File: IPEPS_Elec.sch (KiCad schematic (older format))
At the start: 34 parts

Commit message: replace the OR gate by transistors
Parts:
- removed U?: CD74HCT4075E, symbol 74xGxx:74LVC1G332
- added Q? (x2): BC547, Package_TO_SOT_THT:TO-92_Inline, symbol Transistor_BJT:BC547
- added R? (x4): 47k, symbol Device:R_Small
- added R?: 100k, symbol Device:R_Small
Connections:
- wire segments 74 -> 78
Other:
- moved on the sheet: BT?, C?, D?, Q?, R?, SW?, U?A, U?B

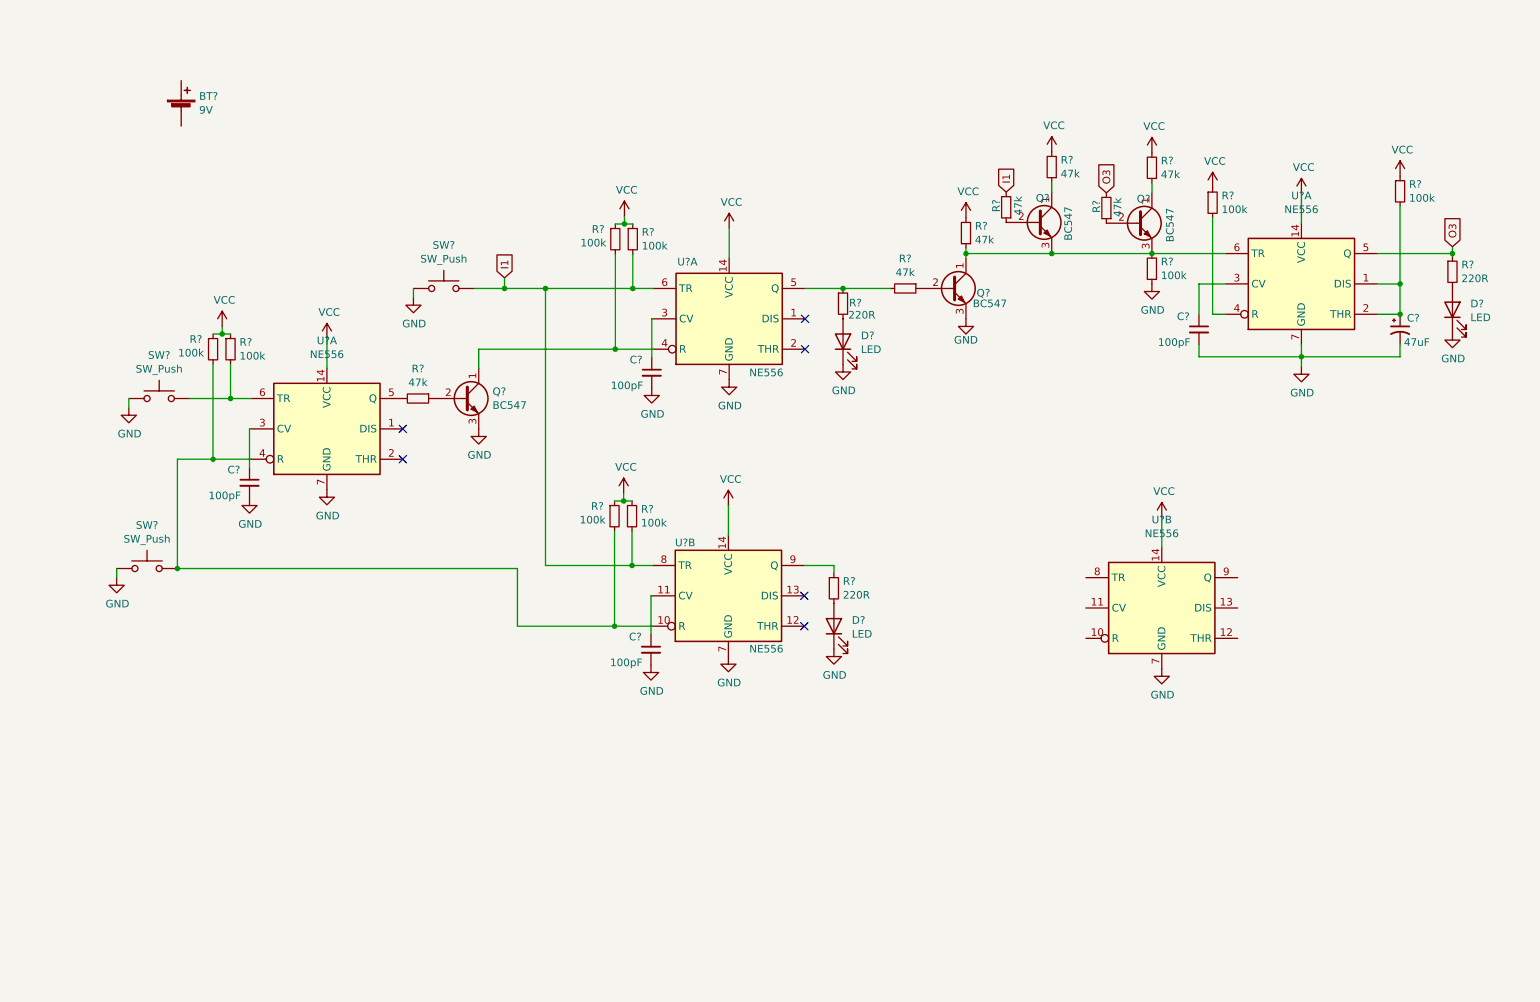
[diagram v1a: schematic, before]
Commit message: remove TTL gates and wire up the astable 555
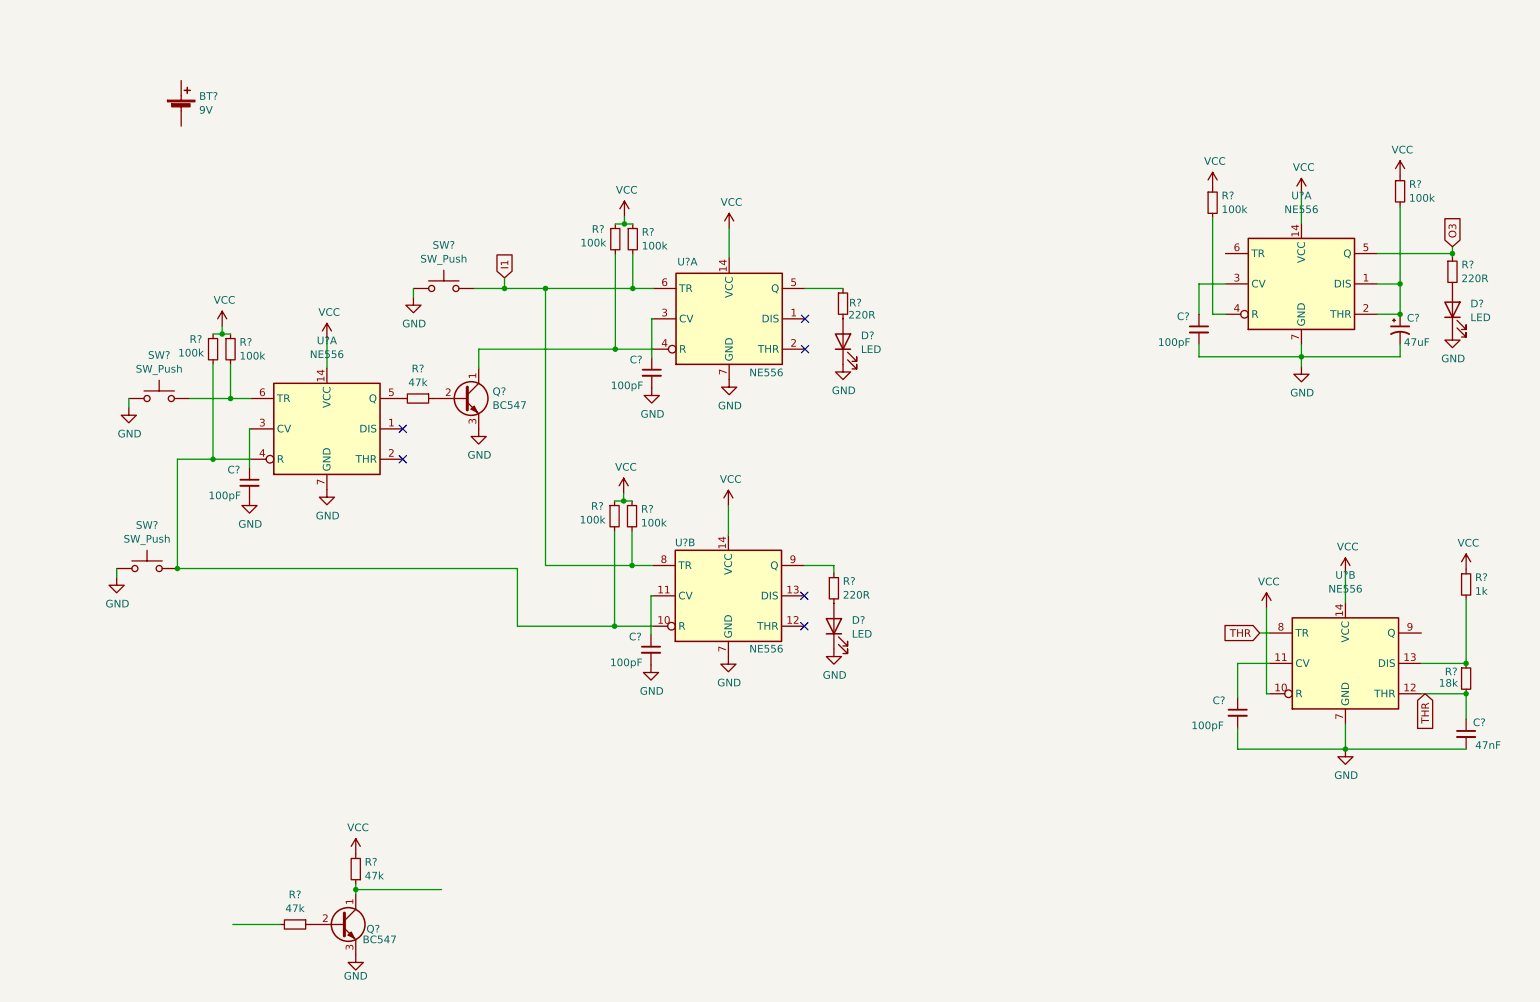
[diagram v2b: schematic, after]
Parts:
- removed Q? (x2): BC547, Package_TO_SOT_THT:TO-92_Inline, symbol Transistor_BJT:BC547
- removed R? (x4): 47k, symbol Device:R_Small
- removed R?: 100k, symbol Device:R_Small
- added C?: 47nF, symbol Device:C_Small
- added C?: 100pF, symbol Device:C_Small
- added R?: 1k, symbol Device:R_Small
- added R?: 18k, symbol Device:R_Small
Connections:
- net GND: now also C?.2, C?.2
- net VCC: now also U?.10 (R), R?.1
- net at R?.1, U?.5 (Q): no longer R?.2
- net at U?.11 (CV): now also C?.1
- net THR: now reaches U?.12 (THR)
- net THR: now also U?.8 (TR), C?.1, R?.2
- net at U?.13 (DIS): now also R?.1, R?.2
- net at Q?.1 (C), R?.1: no longer U?.6 (TR)
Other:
- moved on the sheet: Q?, R?, U?B

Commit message: wire up the tc4428 + add buzzer + wire OR gate
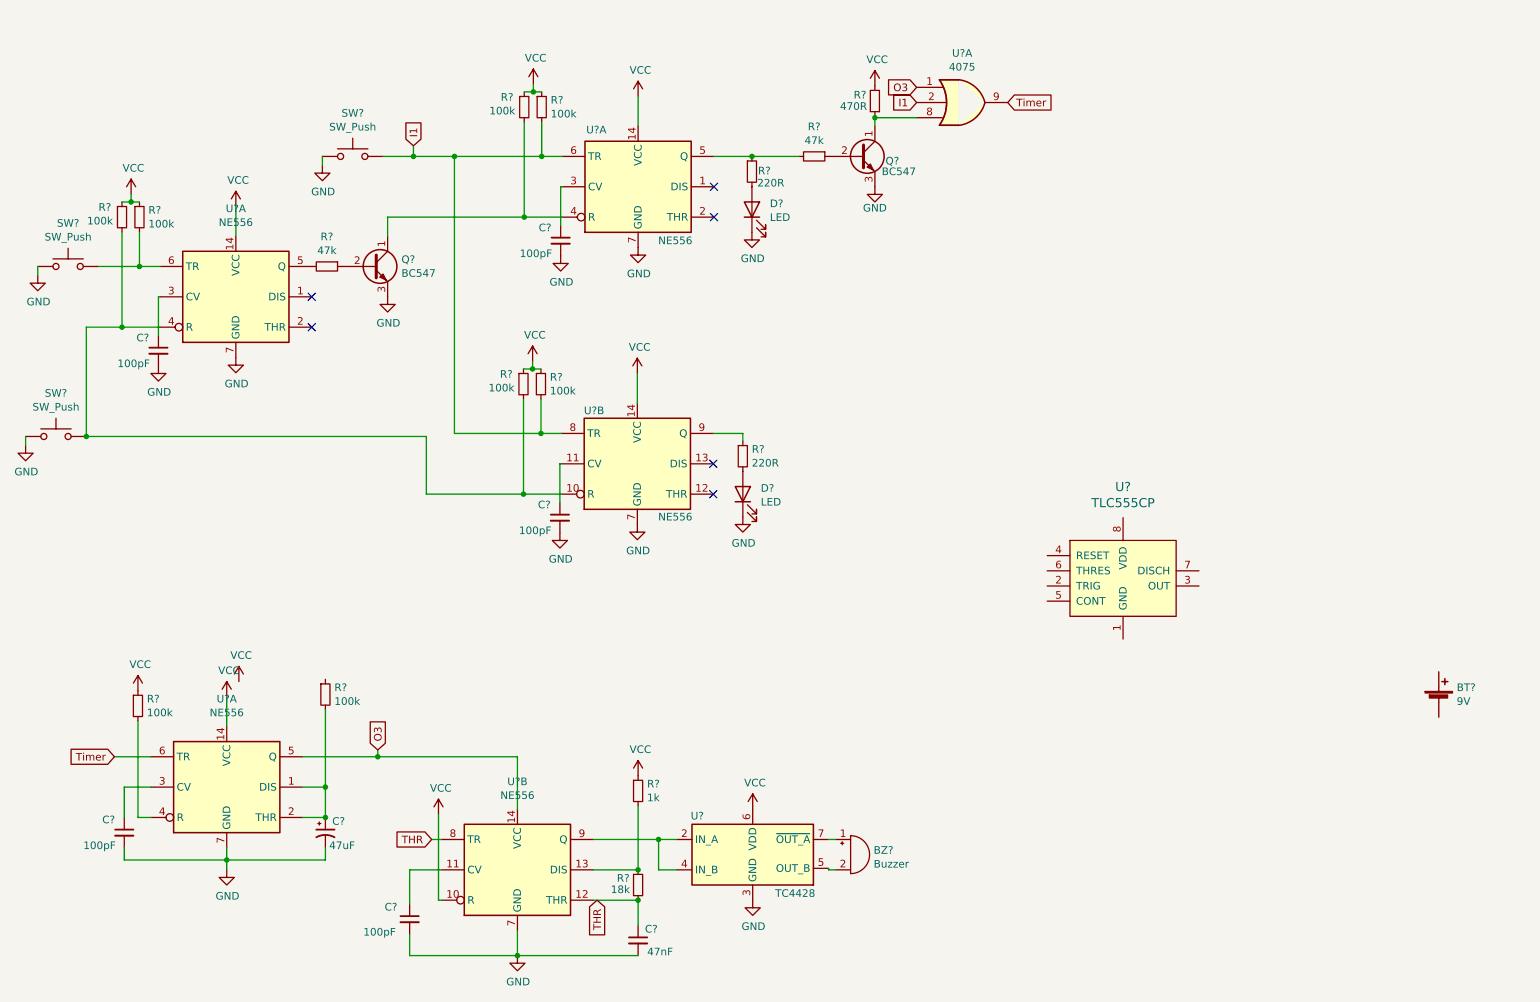
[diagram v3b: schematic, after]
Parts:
- removed D?: LED, symbol Device:LED
- removed R?: 220R, symbol Device:R_Small
- added BZ?: Buzzer, symbol Device:Buzzer
- added U?: TC4428, Package_DIP:DIP-8_W7.62mm, symbol labo2:TC4428
- added U?: 4075, symbol 4xxx:4075
- added U?: TLC555CP, digikey-footprints:DIP-8_W7.62mm, symbol dk_Clock-Timing-Programmable-Timers-and-Oscillators:TLC555CP
- R?: value 47k -> 470R
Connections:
- net GND: now also U?.3 (GND)
- net I1: now also U?.2
- net O3: now also U?.14 (VCC), U?.1
- net VCC: now also U?.6 (VDD); no longer R?.1, U?.14 (VCC)
- net at R?.1, U?.5 (Q): now also R?.2
- net at U?.9 (Q): now also U?.2 (IN_A), U?.4 (IN_B)
- net Timer: now reaches U?.6 (TR)
- net Timer: now also U?.9
- net at Q?.1 (C), R?.1: now also U?.8
- new net: U?.1 (NC), U?.8 (NC)
- new net: BZ?.2 (+), U?.5 (OUT_B)
- new net: BZ?.1 (-), U?.7 (~OUT_A)
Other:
- moved on the sheet: BT?, C?, D?, Q?, R?, SW?, U?A, U?B

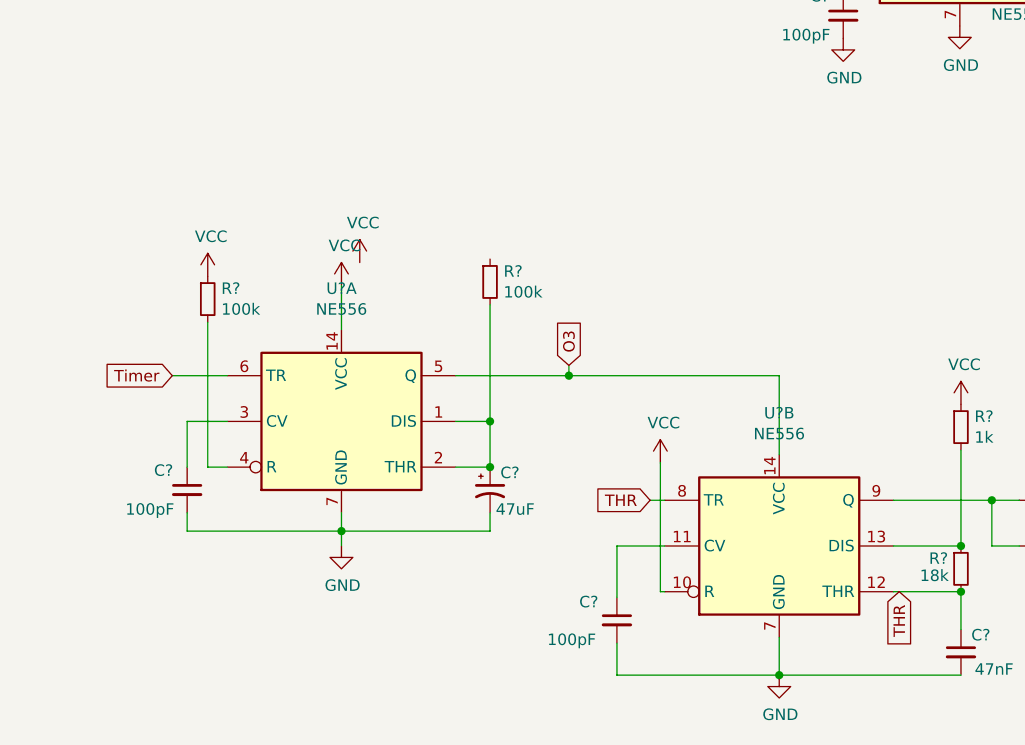
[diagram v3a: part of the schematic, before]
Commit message: add an NPN to power up astable
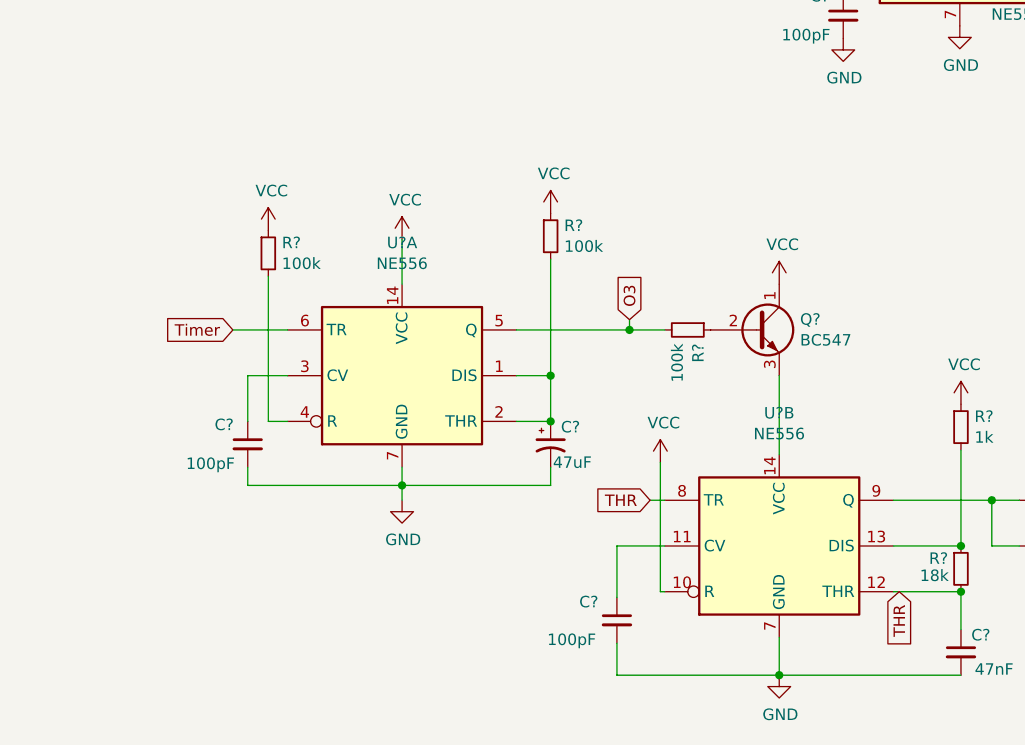
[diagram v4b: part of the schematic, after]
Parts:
- added Q?: BC547, Package_TO_SOT_THT:TO-92_Inline, symbol Transistor_BJT:BC547
- added R?: 100k, symbol Device:R_Small
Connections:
- net O3: now also R?.2; no longer U?.14 (VCC)
- net VCC: now also R?.1, Q?.1 (C)
- new net: Q?.3 (E), U?.14 (VCC)
- new net: Q?.2 (B), R?.1
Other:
- moved on the sheet: C?, R?, U?A
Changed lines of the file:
@@
 L Timer:NE556 U?
 U 1 1 61904F77
-P 2070 5820
-F 0 "U?" H 2070 6401 50  0000 C CNN
-F 1 "NE556" H 2070 6310 50  0000 C CNN
-F 2 "" H 2070 5820 50  0001 C CNN
-F 3 "http://www.ti.com/lit/ds/symlink/ne556.pdf" H 2070 5820 50  0001 C CNN
-	1    2070 5820
+P 2335 5620
+F 0 "U?" H 2335 6201 50  0000 C CNN
+F 1 "NE556" H 2335 6110 50  0000 C CNN
+F 2 "" H 2335 5620 50  0001 C CNN
+F 3 "http://www.ti.com/lit/ds/symlink/ne556.pdf" H 2335 5620 50  0001 C CNN
+	1    2335 5620
 	1    0    0    -1
 $EndComp
@@
 L power:VCC #PWR?
 U 1 1 61936BE9
-P 2070 5225
-F 0 "#PWR?" H 2070 5075 50  0001 C CNN
-F 1 "VCC" H 2085 5398 50  0000 C CNN
-F 2 "" H 2070 5225 50  0001 C CNN
-F 3 "" H 2070 5225 50  0001 C CNN
-	1    2070 5225
-	1    0    0    -1
-$EndComp
-Wire Wire Line
-	2070 5420 2070 5225
+P 2335 5025
+F 0 "#PWR?" H 2335 4875 50  0001 C CNN
+F 1 "VCC" H 2350 5198 50  0000 C CNN
+F 2 "" H 2335 5025 50  0001 C CNN
+F 3 "" H 2335 5025 50  0001 C CNN
+	1    2335 5025
+	1    0    0    -1
+$EndComp
+Wire Wire Line
+	2335 5220 2335 5025
 $Comp
 L power:GND #PWR?
@@
 L power:GND #PWR?
 U 1 1 6193C618
-P 2070 6365
-F 0 "#PWR?" H 2070 6115 50  0001 C CNN
-F 1 "GND" H 2075 6192 50  0000 C CNN
-F 2 "" H 2070 6365 50  0001 C CNN
-F 3 "" H 2070 6365 50  0001 C CNN
-	1    2070 6365
+P 2335 6165
+F 0 "#PWR?" H 2335 5915 50  0001 C CNN
+F 1 "GND" H 2340 5992 50  0000 C CNN
+F 2 "" H 2335 6165 50  0001 C CNN
+F 3 "" H 2335 6165 50  0001 C CNN
+	1    2335 6165
 	1    0    0    -1
 $EndComp
@@
 L Device:R_Small R?
 U 1 1 619EB70F
-P 2720 5210
-F 0 "R?" H 2779 5256 50  0000 L CNN
-F 1 "100k" H 2779 5165 50  0000 L CNN
-F 2 "" H 2720 5210 50  0001 C CNN
-F 3 "~" H 2720 5210 50  0001 C CNN
-	1    2720 5210
+P 2985 5010
+F 0 "R?" H 3044 5056 50  0000 L CNN
+F 1 "100k" H 3044 4965 50  0000 L CNN
+F 2 "" H 2985 5010 50  0001 C CNN
+F 3 "~" H 2985 5010 50  0001 C CNN
+	1    2985 5010
 	1    0    0    -1
 $EndComp
@@
 L power:VCC #PWR?
 U 1 1 619EC41F
-P 2150 5125
-F 0 "#PWR?" H 2150 4975 50  0001 C CNN
-F 1 "VCC" H 2165 5298 50  0000 C CNN
-F 2 "" H 2150 5125 50  0001 C CNN
-F 3 "" H 2150 5125 50  0001 C CNN
-	1    2150 5125
-	1    0    0    -1
-$EndComp
-Wire Wire Line
-	2570 5820 2720 5820
-Wire Wire Line
-	2720 5310 2720 5820
-Wire Wire Line
-	2570 6020 2720 6020
-Wire Wire Line
-	2720 6020 2720 5820
-Connection ~ 2720 5820
+P 2985 4910
+F 0 "#PWR?" H 2985 4760 50  0001 C CNN
+F 1 "VCC" H 3000 5083 50  0000 C CNN
+F 2 "" H 2985 4910 50  0001 C CNN
+F 3 "" H 2985 4910 50  0001 C CNN
+	1    2985 4910
+	1    0    0    -1
+$EndComp
+Wire Wire Line
+	2835 5620 2985 5620
+Wire Wire Line
+	2985 5110 2985 5620
+Wire Wire Line
+	2835 5820 2985 5820
+Wire Wire Line
+	2985 5820 2985 5620
+Connection ~ 2985 5620
 $Comp
 L Device:CP1_Small C?
 U 1 1 619F6519
-P 2720 6120
-F 0 "C?" H 2765 6195 50  0000 L CNN
-F 1 "47uF" H 2745 6035 50  0000 L CNN
-F 2 "" H 2720 6120 50  0001 C CNN
-F 3 "~" H 2720 6120 50  0001 C CNN
-	1    2720 6120
-	1    0    0    -1
-$EndComp
-Connection ~ 2720 6020
+P 2985 5920
+F 0 "C?" H 3030 5995 50  0000 L CNN
+F 1 "47uF" H 2995 5840 50  0000 L CNN
+F 2 "" H 2985 5920 50  0001 C CNN
+F 3 "~" H 2985 5920 50  0001 C CNN
+	1    2985 5920
+	1    0    0    -1
+$EndComp
+Connection ~ 2985 5820
 $Comp
 L Device:C_Small C?
 U 1 1 619FB1EC
-P 1395 6120
-F 0 "C?" H 1250 6205 50  0000 L CNN
-F 1 "100pF" H 1125 6035 50  0000 L CNN
-F 2 "" H 1395 6120 50  0001 C CNN
-F 3 "~" H 1395 6120 50  0001 C CNN
-	1    1395 6120
-	1    0    0    -1
-$EndComp
-Wire Wire Line
-	2070 6220 2070 6300
-Wire Wire Line
-	2720 6220 2720 6300
-Wire Wire Line
-	2720 6300 2070 6300
-Connection ~ 2070 6300
-Wire Wire Line
-	2070 6300 2070 6365
-Wire Wire Line
-	1395 6220 1395 6300
-Wire Wire Line
-	1395 6300 2070 6300
-Wire Wire Line
-	1570 5820 1395 5820
-Wire Wire Line
-	1395 5820 1395 6020
-Wire Wire Line
-	1570 6020 1485 6020
-Wire Wire Line
-	1485 6020 1485 5385
+P 1660 5920
+F 0 "C?" H 1515 6005 50  0000 L CNN
+F 1 "100pF" H 1390 5835 50  0000 L CNN
+F 2 "" H 1660 5920 50  0001 C CNN
+F 3 "~" H 1660 5920 50  0001 C CNN
+	1    1660 5920
+	1    0    0    -1
+$EndComp
+Wire Wire Line
+	2335 6020 2335 6100
+Wire Wire Line
+	2985 6020 2985 6100
+Wire Wire Line
+	2985 6100 2335 6100
+Connection ~ 2335 6100
+Wire Wire Line
+	2335 6100 2335 6165
+Wire Wire Line
+	1660 6020 1660 6100
+Wire Wire Line
+	1660 6100 2335 6100
+Wire Wire Line
+	1835 5620 1660 5620
+Wire Wire Line
+	1660 5620 1660 5820
+Wire Wire Line
+	1835 5820 1750 5820
+Wire Wire Line
+	1750 5820 1750 5185
 $Comp
 L power:VCC #PWR?
 U 1 1 61A07F28
-P 1485 5185
-F 0 "#PWR?" H 1485 5035 50  0001 C CNN
-F 1 "VCC" H 1500 5358 50  0000 C CNN
-F 2 "" H 1485 5185 50  0001 C CNN
-F 3 "" H 1485 5185 50  0001 C CNN
-	1    1485 5185
+P 1750 4985
+F 0 "#PWR?" H 1750 4835 50  0001 C CNN
+F 1 "VCC" H 1765 5158 50  0000 C CNN
+F 2 "" H 1750 4985 50  0001 C CNN
+F 3 "" H 1750 4985 50  0001 C CNN
+	1    1750 4985
 	1    0    0    -1
 $EndComp
@@
 L Device:R_Small R?
 U 1 1 61A2A7B2
-P 1485 5285
-F 0 "R?" H 1544 5331 50  0000 L CNN
-F 1 "100k" H 1544 5240 50  0000 L CNN
-F 2 "" H 1485 5285 50  0001 C CNN
-F 3 "~" H 1485 5285 50  0001 C CNN
-	1    1485 5285
+P 1750 5085
+F 0 "R?" H 1809 5131 50  0000 L CNN
+F 1 "100k" H 1809 5040 50  0000 L CNN
+F 2 "" H 1750 5085 50  0001 C CNN
+F 3 "~" H 1750 5085 50  0001 C CNN
+	1    1750 5085
 	1    0    0    -1
 $EndComp
@@
 	1    0    0    -1
 $EndComp
-Text GLabel 3065 5575 1    50   Input ~ 0
+Text GLabel 3330 5375 1    50   Input ~ 0
 O3
 Wire Wire Line
@@
 	1    0    0    -1
 $EndComp
-Wire Wire Line
-	2570 5620 3065 5620
-Wire Wire Line
-	3065 5575 3065 5620
-Connection ~ 3065 5620
-Wire Wire Line
-	3065 5620 3985 5620
 Text GLabel 6615 1210 0    50   Input ~ 0
 O3
@@
 Text GLabel 7215 1310 2    50   Input ~ 0
 Timer
-Text GLabel 1330 5620 0    50   Input ~ 0
+Text GLabel 1595 5420 0    50   Input ~ 0
 Timer
 Wire Wire Line
-	1330 5620 1570 5620
+	1595 5420 1835 5420
 $Comp
 L dk_Clock-Timing-Programmable-Timers-and-Oscillators:TLC555CP U?
@@
 	1    0    0    -1
 $EndComp
+$Comp
+L Transistor_BJT:BC547 Q?
+U 1 1 6197B7D5
+P 3885 5420
+F 0 "Q?" H 4076 5466 50  0000 L CNN
+F 1 "BC547" H 4076 5375 50  0000 L CNN
+F 2 "Package_TO_SOT_THT:TO-92_Inline" H 4085 5345 50  0001 L CIN
+F 3 "https://www.onsemi.com/pub/Collateral/BC550-D.pdf" H 3885 5420 50  0001 L CNN
+	1    3885 5420
+	1    0    0    -1
+$EndComp
+$Comp
+L power:VCC #PWR?
+U 1 1 6197D552
+P 3985 5220
+F 0 "#PWR?" H 3985 5070 50  0001 C CNN
+F 1 "VCC" H 4000 5393 50  0000 C CNN
+F 2 "" H 3985 5220 50  0001 C CNN
+F 3 "" H 3985 5220 50  0001 C CNN
+	1    3985 5220
+	1    0    0    -1
+$EndComp
+Wire Wire Line
+	2835 5420 3330 5420
+Wire Wire Line
+	3330 5375 3330 5420
+$Comp
+L Device:R_Small R?
+U 1 1 6199A848
+P 3585 5420
+F 0 "R?" H 3644 5466 50  0000 L CNN
+F 1 "100k" H 3644 5375 50  0000 L CNN
+F 2 "" H 3585 5420 50  0001 C CNN
+F 3 "~" H 3585 5420 50  0001 C CNN
+	1    3585 5420
+	0    1    1    0
+$EndComp
+Wire Wire Line
+	3485 5420 3330 5420
+Connection ~ 3330 5420
 $EndSCHEMATC
